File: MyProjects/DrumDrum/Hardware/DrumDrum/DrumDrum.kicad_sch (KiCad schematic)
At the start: 76 parts, among them J1 GATE, J2 CV_1, J3 CV_2, J4 CV_3, J5 CV_4, J5 Conn_02x05_Odd_Even, J6 CV_OUT, J7 CV_INV_OUT, J8 OUT_1, Q1 2N3904, SW1 SW_Push, SW2 SW_Push, U1 TL074, U2 MCP6004, U3 LM4040DBZ-10

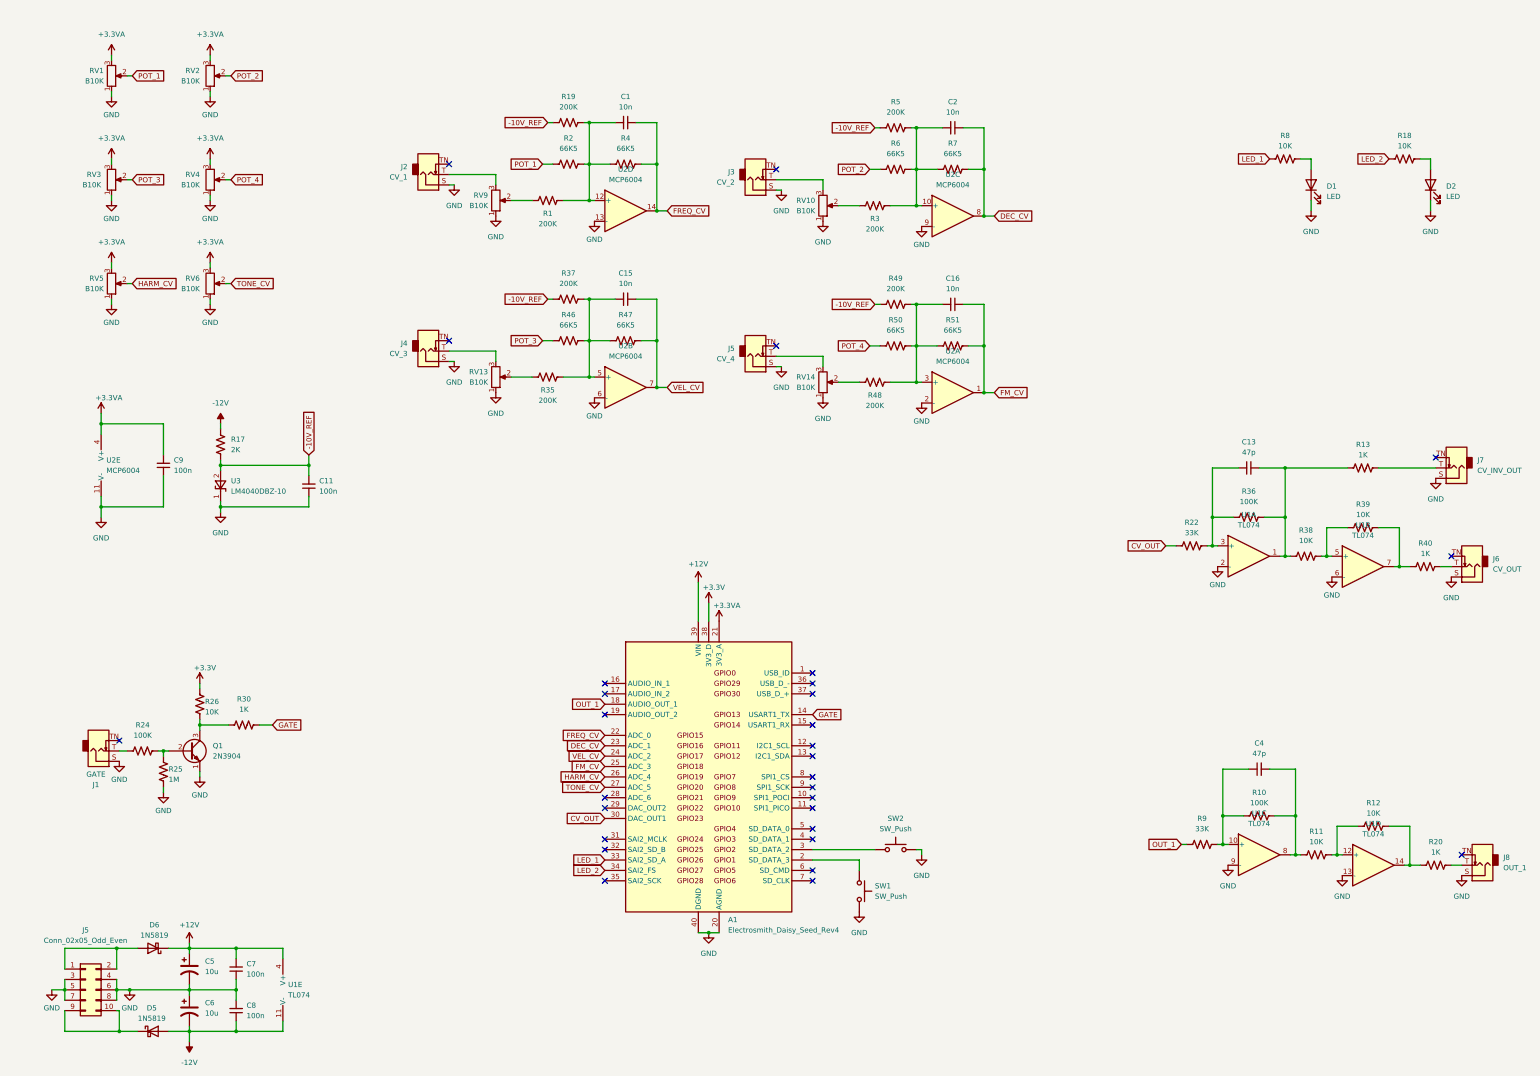
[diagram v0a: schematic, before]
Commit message: Update DrumDrum schematic
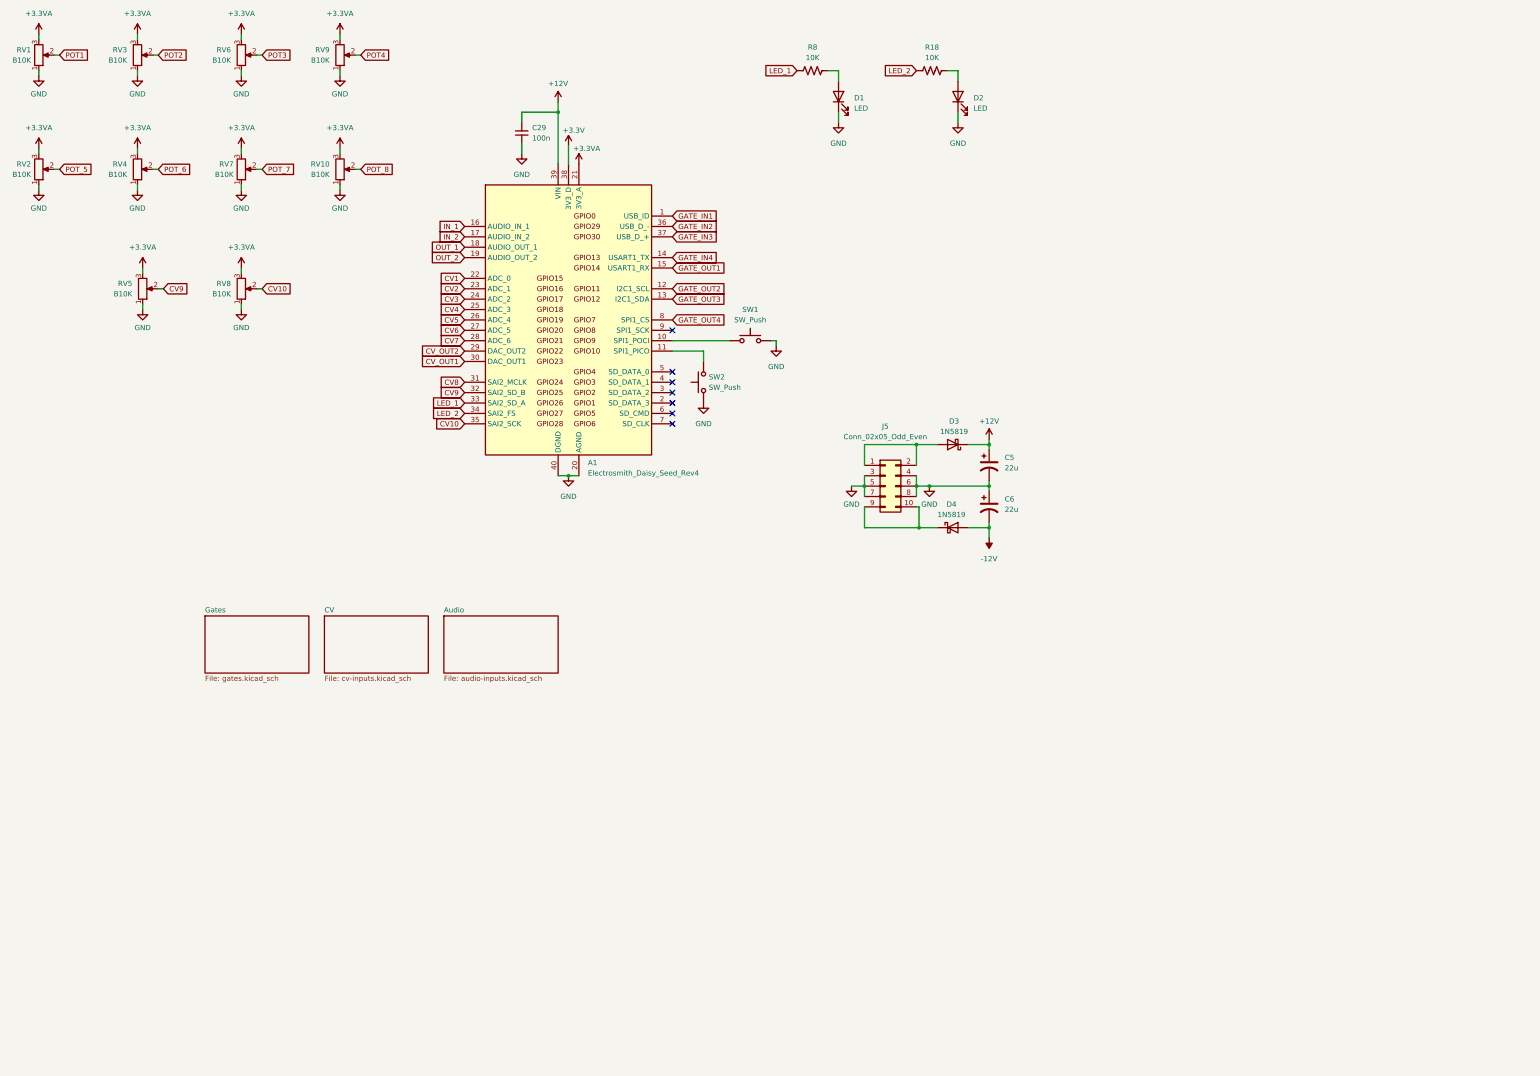
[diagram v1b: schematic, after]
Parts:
- removed C1, C15, C16, C2: 10n, Capacitor_SMD:C_0805_2012Metric_Pad1.18x1.45mm_HandSolder, symbol Device:C_Small
- removed C11, C7, C8, C9: 100n, Capacitor_SMD:C_0805_2012Metric_Pad1.18x1.45mm_HandSolder, symbol Device:C_Small
- removed C13, C4: 47p, Capacitor_SMD:C_0805_2012Metric_Pad1.18x1.45mm_HandSolder, symbol Device:C_Small
- removed D5, D6: 1N5819, Diode_THT:D_DO-41_SOD81_P10.16mm_Horizontal, symbol Diode:1N5819
- removed J1: GATE, symbol Connector_Audio:AudioJack2_SwitchT
- removed J2: CV_1, symbol Connector_Audio:AudioJack2_SwitchT
- removed J3: CV_2, symbol Connector_Audio:AudioJack2_SwitchT
- removed J4: CV_3, symbol Connector_Audio:AudioJack2_SwitchT
- removed J5: CV_4, symbol Connector_Audio:AudioJack2_SwitchT
- removed J6: CV_OUT, symbol Connector_Audio:AudioJack2_SwitchT
- removed J7: CV_INV_OUT, symbol Connector_Audio:AudioJack2_SwitchT
- removed J8: OUT_1, symbol Connector_Audio:AudioJack2_SwitchT
- removed Q1: 2N3904, Package_TO_SOT_THT:TO-92_Inline, symbol Transistor_BJT:2N3904
- removed R1, R19, R3, R35, R37, R48, R49, R5: 200K, Resistor_THT:R_Axial_DIN0207_L6.3mm_D2.5mm_P7.62mm_Horizontal, symbol Device:R_US
- removed R10, R24, R36: 100K, Resistor_THT:R_Axial_DIN0207_L6.3mm_D2.5mm_P7.62mm_Horizontal, symbol Device:R_US
- removed R11, R12, R26, R38, R39: 10K, Resistor_THT:R_Axial_DIN0207_L6.3mm_D2.5mm_P7.62mm_Horizontal, symbol Device:R_US
- removed R13, R20, R30, R40: 1K, Resistor_THT:R_Axial_DIN0207_L6.3mm_D2.5mm_P7.62mm_Horizontal, symbol Device:R_US
- removed R17: 2K, Resistor_THT:R_Axial_DIN0207_L6.3mm_D2.5mm_P7.62mm_Horizontal, symbol Device:R_US
- removed R2, R4, R46, R47, R50, R51, R6, R7: 66K5, Resistor_THT:R_Axial_DIN0207_L6.3mm_D2.5mm_P7.62mm_Horizontal, symbol Device:R_US
- removed R22, R9: 33K, Resistor_THT:R_Axial_DIN0207_L6.3mm_D2.5mm_P7.62mm_Horizontal, symbol Device:R_US
- removed R25: 1M, Resistor_THT:R_Axial_DIN0207_L6.3mm_D2.5mm_P7.62mm_Horizontal, symbol Device:R_US
- removed RV13, RV14: B10K, Potentiometer_THT:Potentiometer_TT_P0915N, symbol Device:R_Potentiometer
- removed U1: TL074, Package_DIP:DIP-14_W7.62mm_Socket_LongPads, symbol Amplifier_Operational:TL074
- removed U2: MCP6004, Package_DIP:DIP-14_W7.62mm_Socket_LongPads, symbol Amplifier_Operational:MCP6004
- removed U3: LM4040DBZ-10, Package_TO_SOT_SMD:SOT-23, symbol Reference_Voltage:LM4040DBZ-10
- added C29: 100n, Capacitor_SMD:C_0805_2012Metric_Pad1.18x1.45mm_HandSolder, symbol Device:C_Small
- added D3, D4: 1N5819, Diode_THT:D_DO-41_SOD81_P10.16mm_Horizontal, symbol Diode:1N5819
- added RV7, RV8: B10K, Potentiometer_THT:Potentiometer_TT_P0915N, symbol Device:R_Potentiometer
- C5, C6: value 10u -> 22u
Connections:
- net +12V: now also C29.2, D3.1 (K)
- net +3.3VA: now also RV10.3, RV9.3, RV7.3, RV8.3
- net -12V: now also D4.2 (A)
- net GND: now also SW2.1, C29.1, RV7.1, RV8.1; no longer SW2.2
- net GATE_IN1: now reaches A1.1 (USB_ID)
- net at A1.10 (SPI1_POCI): now also SW1.1
- net at A1.11 (SPI1_PICO): now also SW2.2
- net GATE_OUT2: now reaches A1.12 (I2C1_SCL)
- net GATE_OUT3: now reaches A1.13 (I2C1_SDA)
- net GATE_OUT1: now reaches A1.15 (USART1_RX)
- net IN_1: now reaches A1.16 (AUDIO_IN_1)
- net IN_2: now reaches A1.17 (AUDIO_IN_2)
- net OUT_2: now reaches A1.19 (AUDIO_OUT_2)
- net at A1.2 (SD_DATA_3): no longer SW1.1
- net CV7: now reaches A1.28 (ADC_6)
- net CV_OUT2: now reaches A1.29 (DAC_OUT2)
- net at A1.3 (SD_DATA_2): no longer SW2.1
- net CV8: now reaches A1.31 (SAI2_MCLK)
- net CV9: now reaches A1.32 (SAI2_SD_B)
- net CV9: now also RV5.2
- net CV10: now reaches A1.35 (SAI2_SCK)
- net CV10: now also RV8.2
- net GATE_IN2: now reaches A1.36 (USB_D_-)
- net GATE_IN3: now reaches A1.37 (USB_D_+)
- net GATE_OUT4: now reaches A1.8 (SPI1_CS)
- net POT_8: now reaches RV10.2
- net POT4: now reaches RV9.2
- net at J5.1 (Pin_1), J5.2 (Pin_2): now also D3.2 (A)
- net at J5.10 (Pin_10), J5.9 (Pin_9): now also D4.1 (K)
- net CV_OUT renamed CV_OUT1
- net DEC_CV renamed CV2
- net FM_CV renamed CV4
- net FREQ_CV renamed CV1
- net GATE renamed GATE_IN4
- net HARM_CV renamed CV5
- net CV5: no longer RV5.2
- net POT_1 renamed POT1
- net POT_2 renamed POT_5
- net POT_3 renamed POT2
- net POT_4 renamed POT_6
- net TONE_CV renamed CV6
- net CV6: no longer RV6.2
- net VEL_CV renamed CV3
- new net POT3: RV6.2
- new net POT_7: RV7.2
- no-connect marks 30 -> 7
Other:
- added sheet Audio (audio-inputs.kicad_sch)
- added sheet CV (cv-inputs.kicad_sch)
- added sheet Gates (gates.kicad_sch)
- moved on the sheet: A1, D1, D2, R18, R8
